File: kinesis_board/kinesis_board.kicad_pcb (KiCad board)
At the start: 0 parts

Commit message: finished drawing of the schematics -- needs to be checked before pcb drawing
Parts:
- added 16Mhz1: Crystal, Crystal:Crystal_SMD_HC49-SD_HandSoldering, F.Cu at (146.3, 96.3)
- added C1: 27p, Connector_JST:JST_PH_S7B-PH-K_1x07_P2.00mm_Horizontal, F.Cu at (138.6, 66.6)
- added C2: 27p, Capacitor_SMD:C_0805_2012Metric_Pad1.18x1.45mm_HandSolder, F.Cu at (160.7, 65.8)
- added C3: 100n, Capacitor_SMD:C_0805_2012Metric_Pad1.18x1.45mm_HandSolder, F.Cu at (160.7, 68.8)
- added C4: 4u7, Capacitor_SMD:C_0805_2012Metric_Pad1.18x1.45mm_HandSolder, F.Cu at (160.7, 71.8)
- added C5: 1u, Connector_JST:JST_PH_S7B-PH-K_1x07_P2.00mm_Horizontal, F.Cu at (138.6, 76.3)
- added FB1: FerriteBead, Inductor_SMD:L_0603_1608Metric_Pad1.05x0.95mm_HandSolder, F.Cu at (155.7, 89.4)
- added FB2: FerriteBead, Inductor_SMD:L_0603_1608Metric_Pad1.05x0.95mm_HandSolder, F.Cu at (155.7, 91.9)
- added J2: Conn_01x20, Connector_PinHeader_2.54mm:PinHeader_1x20_P2.54mm_Vertical_SMD_Pin1Left, F.Cu at (123.7, 90.7)
- added J3: Conn_01x20, Connector_PinHeader_2.54mm:PinHeader_1x20_P2.54mm_Vertical_SMD_Pin1Left, F.Cu at (131.6, 90.7)
- added J4: Conn_02x03_Odd_Even, Connector_IDC:IDC-Header_2x03_P2.54mm_Horizontal, F.Cu at (138.5, 105.6)
- added J5: Screw_Terminal_01x02, TerminalBlock_Phoenix:TerminalBlock_Phoenix_MPT-0,5-2-2.54_1x02_P2.54mm_Horizontal, F.Cu at (156.1, 80.2)
- added J6: Conn_01x07, Connector_JST:JST_PH_S7B-PH-K_1x07_P2.00mm_Horizontal, F.Cu at (138.6, 85.9)
- added R1: 68R, Resistor_SMD:R_0805_2012Metric_Pad1.20x1.40mm_HandSolder, F.Cu at (155.9, 65.7)
- added R2: 68R, Resistor_SMD:R_0805_2012Metric_Pad1.20x1.40mm_HandSolder, F.Cu at (155.9, 68.7)
- added R3: 1k5, Resistor_SMD:R_0805_2012Metric_Pad1.20x1.40mm_HandSolder, F.Cu at (155.9, 71.6)
- added R4: 4k7, Resistor_SMD:R_0805_2012Metric_Pad1.20x1.40mm_HandSolder, F.Cu at (155.9, 74.6)
- added TP1: TestPoint, TestPoint:TestPoint_Pad_2.0x2.0mm, F.Cu at (163.2, 78.1)
- added TP2: TestPoint, TestPoint:TestPoint_Pad_2.0x2.0mm, F.Cu at (163.2, 82.1)
- added U1: ATmega16-16A, Package_QFP:TQFP-44_10x10mm_P0.8mm, F.Cu at (160.0, 106.7)
- added U2: D1213A-04S, Package_TO_SOT_SMD:SOT-363_SC-70-6_Handsoldering, F.Cu at (156.5, 86.2)
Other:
- copper layers 0 -> 2

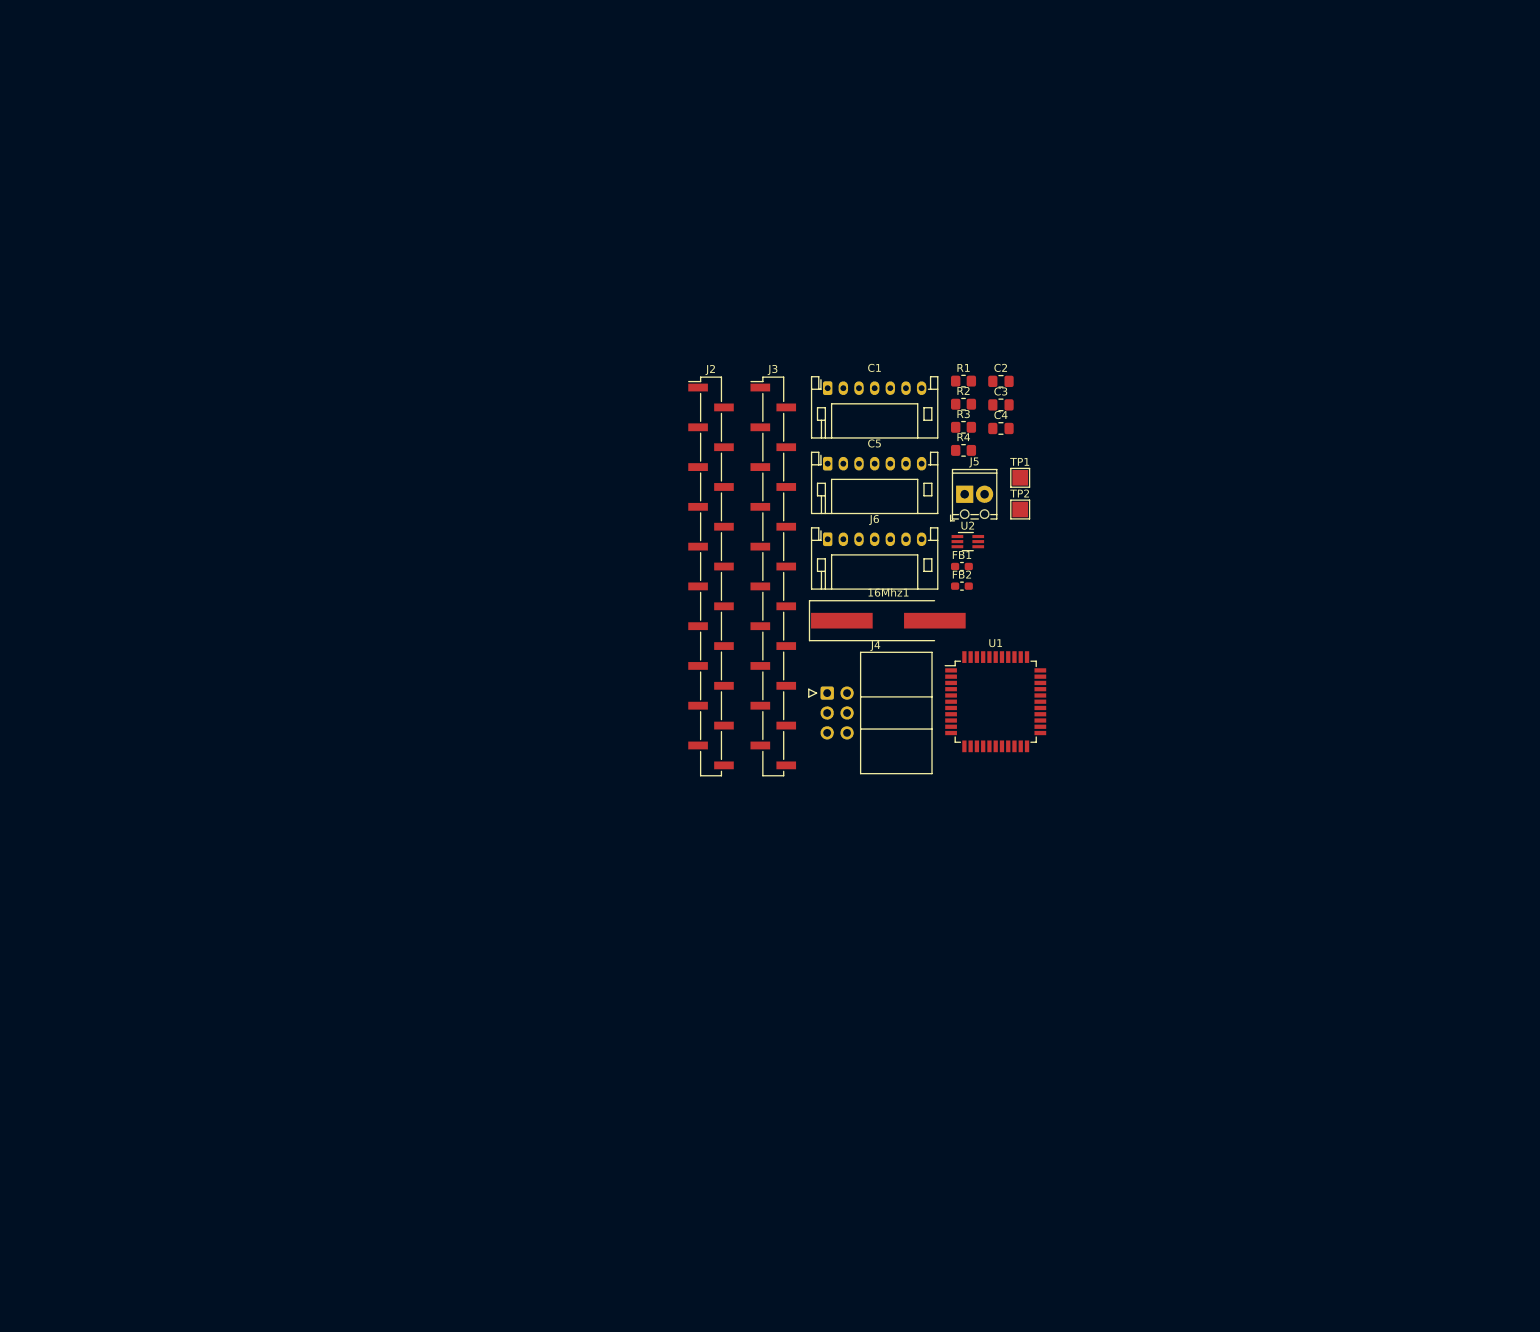
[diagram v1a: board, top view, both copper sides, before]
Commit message: first revision of board - routing needs to be optimized
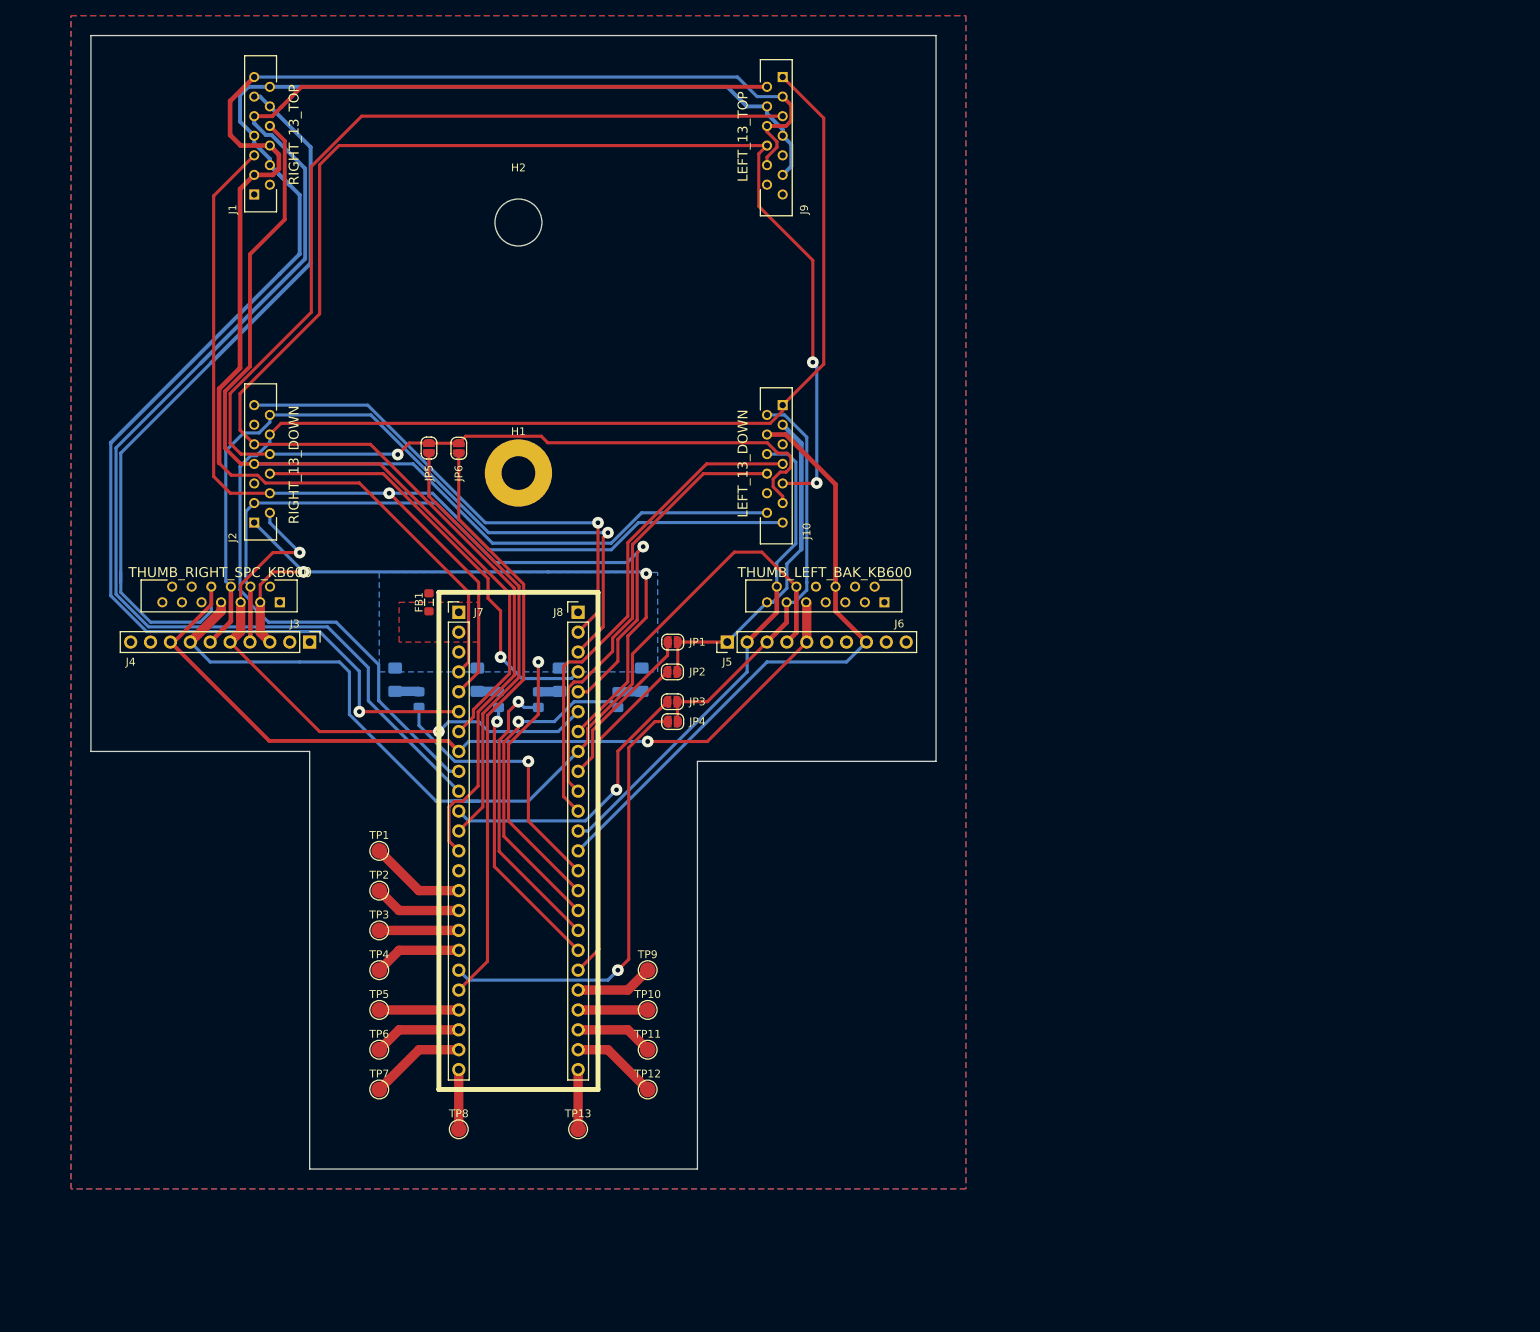
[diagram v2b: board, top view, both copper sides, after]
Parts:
- removed 16Mhz1: Crystal, Crystal:Crystal_SMD_HC49-SD_HandSoldering
- removed C1: 27p, Connector_JST:JST_PH_S7B-PH-K_1x07_P2.00mm_Horizontal
- removed C2: 27p, Capacitor_SMD:C_0805_2012Metric_Pad1.18x1.45mm_HandSolder
- removed C3: 100n, Capacitor_SMD:C_0805_2012Metric_Pad1.18x1.45mm_HandSolder
- removed C4: 4u7, Capacitor_SMD:C_0805_2012Metric_Pad1.18x1.45mm_HandSolder
- removed C5: 1u, Connector_JST:JST_PH_S7B-PH-K_1x07_P2.00mm_Horizontal
- removed FB2: FerriteBead, Inductor_SMD:L_0603_1608Metric_Pad1.05x0.95mm_HandSolder
- removed U1: ATmega16-16A, Package_QFP:TQFP-44_10x10mm_P0.8mm
- removed U2: D1213A-04S, Package_TO_SOT_SMD:SOT-363_SC-70-6_Handsoldering
- added H1: mounting pad, MountingHole:MountingHole_4.3mm_M4_Pad, F.Cu at (99.1, 77.5)
- added H2: mounting pad, MountingHole:MountingHole_6mm, F.Cu at (99.1, 45.5)
- added J1: RIGHT_13_TOP, dodo_conn:Molex-39-53-2135, F.Cu at (65.3, 41.9)
- added J10: LEFT_13_DOWN, dodo_conn:Molex-39-53-2135, F.Cu at (132.8, 68.8)
- added J7: LEFT_1x24, Connector_PinHeader_2.54mm:PinHeader_1x24_P2.54mm_Vertical, F.Cu at (91.4, 95.2)
- added J8: RIGHT_1x24, Connector_PinHeader_2.54mm:PinHeader_1x24_P2.54mm_Vertical, F.Cu at (106.7, 95.2)
- added J9: LEFT_13_TOP, dodo_conn:Molex-39-53-2135, F.Cu at (132.8, 26.9)
- added JP1: SolderJumper_2_Open, Jumper:SolderJumper-2_P1.3mm_Open_RoundedPad1.0x1.5mm, F.Cu at (118.8, 99.1)
- added JP2: SolderJumper_2_Open, Jumper:SolderJumper-2_P1.3mm_Open_RoundedPad1.0x1.5mm, F.Cu at (118.7, 102.9)
- added JP3: SolderJumper_2_Open, Jumper:SolderJumper-2_P1.3mm_Open_RoundedPad1.0x1.5mm, F.Cu at (118.7, 106.7)
- added JP4: SolderJumper_2_Open, Jumper:SolderJumper-2_P1.3mm_Open_RoundedPad1.0x1.5mm, F.Cu at (118.8, 109.2)
- added JP5: SolderJumper_2_Open, Jumper:SolderJumper-2_P1.3mm_Open_RoundedPad1.0x1.5mm, F.Cu at (87.6, 74.3)
- added JP6: SolderJumper_2_Open, Jumper:SolderJumper-2_P1.3mm_Open_RoundedPad1.0x1.5mm, F.Cu at (91.4, 74.3)
- added LED1: LEDSML1206, LED_SMD:LED_1206_3216Metric_Pad1.42x1.75mm_HandSolder, B.Cu at (114.8, 103.9)
- added LED2: LEDSML1206, LED_SMD:LED_1206_3216Metric_Pad1.42x1.75mm_HandSolder, B.Cu at (104.3, 103.9)
- added LED3: LEDSML1206, LED_SMD:LED_1206_3216Metric_Pad1.42x1.75mm_HandSolder, B.Cu at (93.8, 103.9)
- added LED4: LEDSML1206, LED_SMD:LED_1206_3216Metric_Pad1.42x1.75mm_HandSolder, B.Cu at (83.3, 103.9)
- added TP10: TX7, TestPoint:TestPoint_Pad_D2.0mm, F.Cu at (115.6, 146.1)
- added TP11: CRX3, TestPoint:TestPoint_Pad_D2.0mm, F.Cu at (115.6, 151.1)
- added TP12: CTX3, TestPoint:TestPoint_Pad_D2.0mm, F.Cu at (115.6, 156.2)
- added TP13: OUT1B, TestPoint:TestPoint_Pad_D2.0mm, F.Cu at (106.7, 161.3)
- added TP3: A15, TestPoint:TestPoint_Pad_D2.0mm, F.Cu at (81.3, 135.9)
- added TP4: A14, TestPoint:TestPoint_Pad_D2.0mm, F.Cu at (81.3, 141.0)
- added TP5: CS, TestPoint:TestPoint_Pad_D2.0mm, F.Cu at (81.3, 146.1)
- added TP6: TX8, TestPoint:TestPoint_Pad_D2.0mm, F.Cu at (81.3, 151.1)
- added TP7: RX8, TestPoint:TestPoint_Pad_D2.0mm, F.Cu at (81.3, 156.2)
- added TP8: MCLK2, TestPoint:TestPoint_Pad_D2.0mm, F.Cu at (91.4, 161.3)
- added TP9: RX7, TestPoint:TestPoint_Pad_D2.0mm, F.Cu at (115.6, 141.0)
- FB1: footprint Inductor_SMD:L_0603_1608Metric_Pad1.05x0.95mm_HandSolder -> Inductor_SMD:L_0805_2012Metric_Pad1.05x1.20mm_HandSolder
- J2: value Conn_01x20 -> RIGHT_13_DOWN; footprint Connector_PinHeader_2.54mm:PinHeader_1x20_P2.54mm_Vertical_SMD_Pin1Left -> dodo_conn:Molex-39-53-2135
- J3: value Conn_01x20 -> THUMB_RIGHT_SPC_KB600; footprint Connector_PinHeader_2.54mm:PinHeader_1x20_P2.54mm_Vertical_SMD_Pin1Left -> dodo_conn:Molex-39-53-2135
- J4: value Conn_02x03_Odd_Even -> THUMB_RIGHT_SPC; footprint Connector_IDC:IDC-Header_2x03_P2.54mm_Horizontal -> Connector_PinHeader_2.54mm:PinHeader_1x10_P2.54mm_Vertical
- J5: value Screw_Terminal_01x02 -> THUMB_LEFT_BAK; footprint TerminalBlock_Phoenix:TerminalBlock_Phoenix_MPT-0,5-2-2.54_1x02_P2.54mm_Horizontal -> Connector_PinHeader_2.54mm:PinHeader_1x10_P2.54mm_Vertical
- J6: value Conn_01x07 -> THUMB_LEFT_BAK_KB600; footprint Connector_JST:JST_PH_S7B-PH-K_1x07_P2.00mm_Horizontal -> dodo_conn:Molex-39-53-2135
- R1, R2: value 68R -> 10K; moved to B.Cu
- R3: value 1k5 -> 10K; moved to B.Cu
- R4: value 4k7 -> 10K; moved to B.Cu
- TP1: value TestPoint -> A17; footprint TestPoint:TestPoint_Pad_2.0x2.0mm -> TestPoint:TestPoint_Pad_D2.0mm
- TP2: value TestPoint -> A16; footprint TestPoint:TestPoint_Pad_2.0x2.0mm -> TestPoint:TestPoint_Pad_D2.0mm
- moved TP2 95.2 mm to (81.3, 130.8)
- moved TP1 94.7 mm to (81.3, 125.7)
- moved R4 76.5 mm to (86.4, 106.4), turned to 90 degrees
- moved R3 68.8 mm to (96.5, 106.4), turned to 90 degrees
- moved FB1 68.2 mm to (87.6, 94.0), turned to -90 degrees
- moved J4 66.4 mm to (72.4, 99.1), turned to -90 degrees
- moved R2 66.1 mm to (101.6, 106.4), turned to 90 degrees
- moved J3 63.1 mm to (68.6, 94.0), turned to 180 degrees
- moved R1 60.0 mm to (111.8, 106.4), turned to 90 degrees
- moved J2 58.8 mm to (65.3, 83.8), turned to 90 degrees
- moved J5 35.7 mm to (125.7, 99.1), turned to 90 degrees
- moved J6 10.8 mm to (145.8, 94.0), turned to 180 degrees
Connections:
- FB1 pad 1: +5V -> GND
- FB1 pad 2: Net-(J5-Pin_1) -> GNDA
- J2 pad 1: /NUM_LED -> /ROW_6
- J2 pad 10: unconnected-(J2-Pin_10) -> /COL_0
- J2 pad 12: unconnected-(J2-Pin_12) -> /ROW_9
- J2 pad 13: unconnected-(J2-Pin_13) -> /ROW_0
- J2 pad 2: /SCR_LED -> /ROW_8
- J2 pad 3: /KPD_LED -> /ROW_7
- J2 pad 4: /CAPS_LED -> /COL_4
- J2 pad 5: /KPD -> unconnected-(J2-Pin_5)
- J2 pad 6: /PGM -> /ROW_MIN
- J2 pad 7: /EEP_SCL -> /COL_3
- J2 pad 8: /EEP_SDA -> /COL_2
- J2 pad 9: GND -> /COL_1
- J3 pad 1: /MATRIX1 -> unconnected-(J3-Pin_1)
- J3 pad 12: /BUZZER -> unconnected-(J3-Pin_12)
- J3 pad 2: /MATRIX2 -> unconnected-(J3-Pin_2)
- J3 pad 3: /MATRIX3 -> /ROW_6
- J3 pad 4: /MATRIX4 -> /ROW_7
- J3 pad 5: /MATRIX5 -> /ROW_8
- J3 pad 6: /MATRIX6 -> /ROW_9
- J3 pad 7: /MATRIX7 -> /COL_6
- J3 pad 8: /MATRIX8 -> /COL_5
- J4 pad 1: /MISO -> unconnected-(J4-Pin_1)
- J4 pad 2: +5V -> unconnected-(J4-Pin_2)
- J4 pad 3: /SCK -> /ROW_6
- J4 pad 4: /MOSI -> /ROW_7
- J4 pad 5: /RST -> /ROW_8
- J4 pad 6: GND -> /ROW_9
- J5 pad 1: Net-(J5-Pin_1) -> /ROW_4
- J5 pad 2: GND -> /ROW_2
- J6 pad 1: /FS3 -> unconnected-(J6-Pin_1)
- J6 pad 2: Net-(J6-Pin_2) -> unconnected-(J6-Pin_2)
- J6 pad 3: /D+ -> unconnected-(J6-Pin_3)
- J6 pad 4: /D- -> unconnected-(J6-Pin_4)
- J6 pad 5: Net-(J5-Pin_1) -> unconnected-(J6-Pin_5)
- J6 pad 6: /FS1 -> /ROW_3
- J6 pad 7: /FS2 -> unconnected-(J6-Pin_7)
- R1 pad 1: /USB_D- -> /LED_KEYPAD
- R1 pad 2: /D- -> Net-(LED1-K)
- R2 pad 1: /D+ -> /LED_SCROLL_LOCK
- R2 pad 2: /USB_D+ -> Net-(LED2-K)
- R3 pad 1: +5V -> /LED_NUM_LOCK
- R3 pad 2: /D- -> Net-(LED3-K)
- R4 pad 1: +5V -> /LED_CAPS_LOCK
- R4 pad 2: /RST -> Net-(LED4-K)
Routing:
- net /COL_1: track 0.00 -> 228.8 mm, vias 0 -> 2
- net /ROW_F2: track 0.00 -> 213.6 mm, vias 0 -> 1
- net /COL_5: track 0.00 -> 202.4 mm, vias 0 -> 1
- net /ROW_ESC: track 0.00 -> 197.9 mm
- net /ROW_F1: track 0.00 -> 190.8 mm
- net /COL_2: track 0.00 -> 184.6 mm, vias 0 -> 1
- net /COL_3: track 0.00 -> 180.8 mm
- net /COL_0: track 0.00 -> 176.1 mm
- net /COL_4: track 0.00 -> 152.3 mm, vias 0 -> 1
- net /COL_6: track 0.00 -> 125.3 mm
- net /ROW_9: track 0.00 -> 100.1 mm, vias 0 -> 1
- net /ROW_7: track 0.00 -> 94.8 mm, vias 0 -> 1
- net /ROW_6: track 0.00 -> 90.6 mm, vias 0 -> 2
- net /ROW_3: track 0.00 -> 81.0 mm
- net /COL_2_JUMP1: track 0.00 -> 75.4 mm
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- added copper zone on B.Cu, net +3V3
- added copper zone on B.Cu, net GND
- added copper zone on F.Cu, net GND
- added copper zone on F.Cu, net GNDA
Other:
- board outline added: 108 x 144.8 mm

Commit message: adjusted placement of the pin headers and connectors - routing not finished
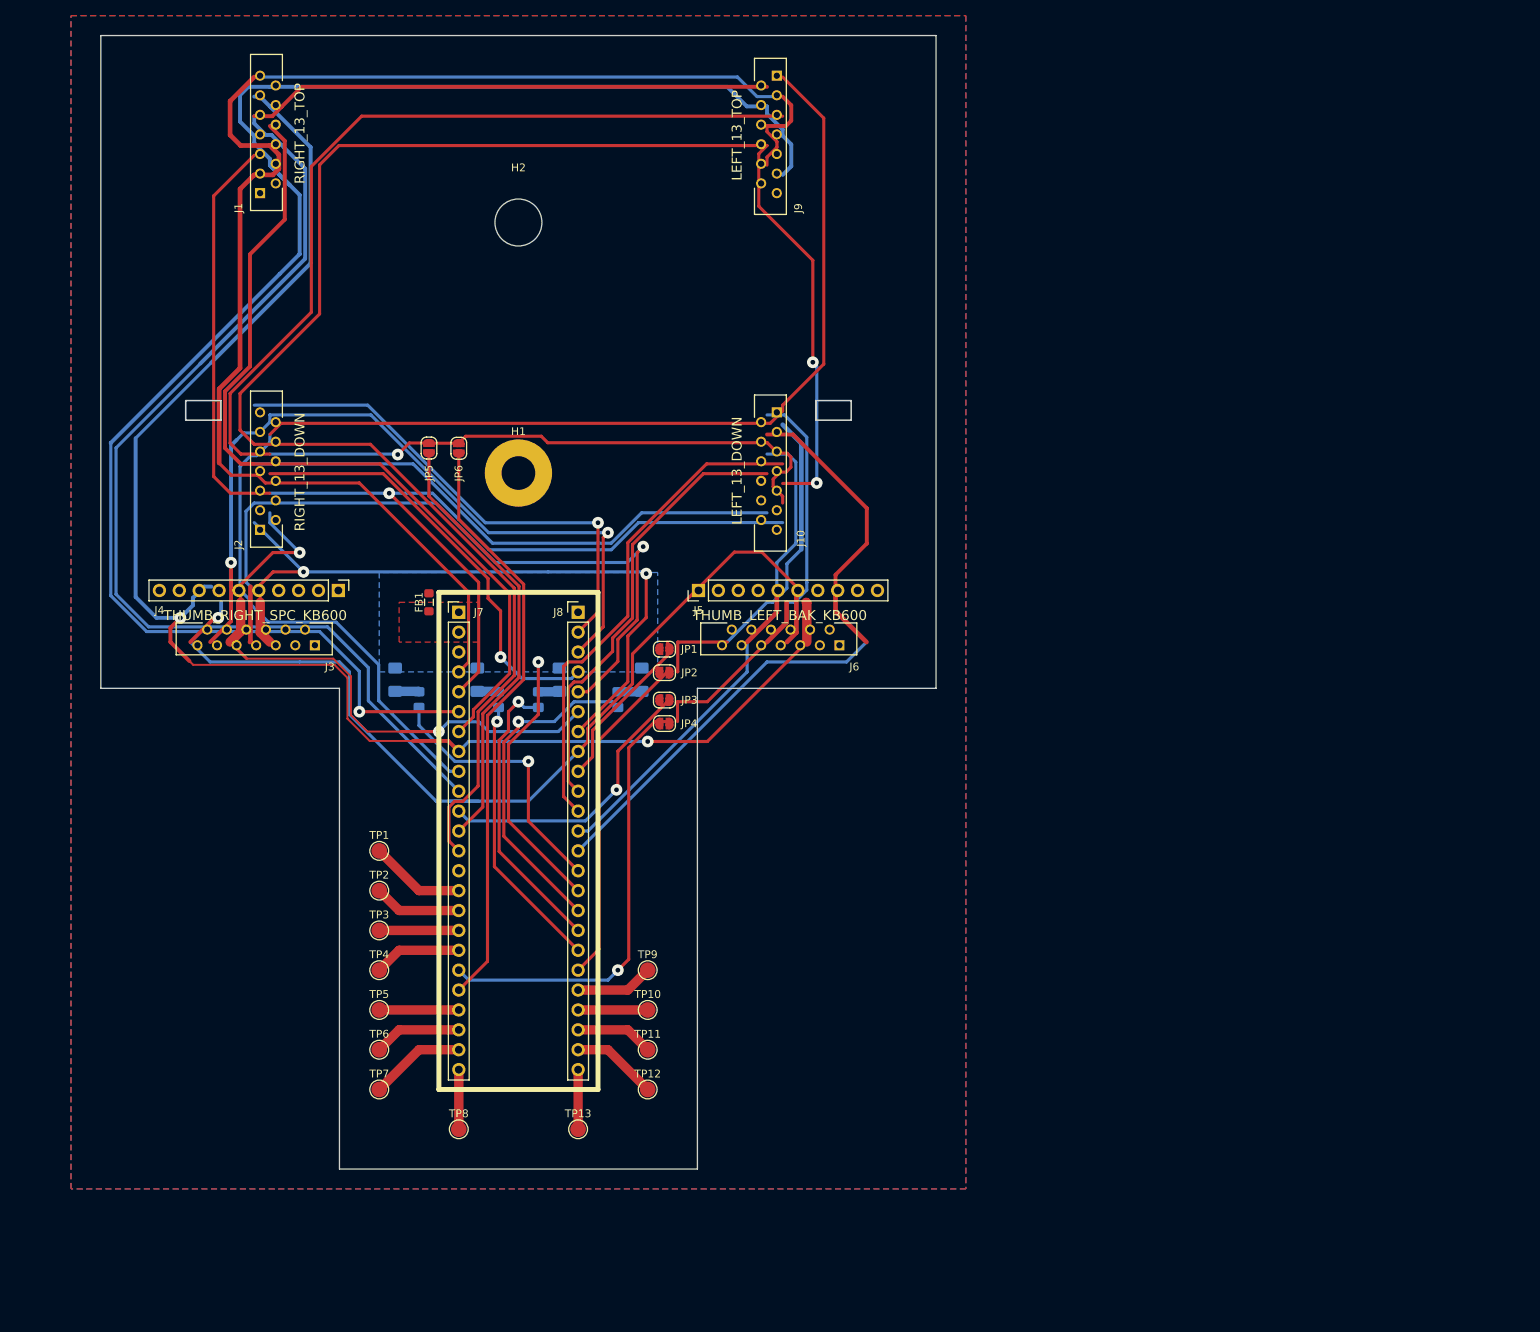
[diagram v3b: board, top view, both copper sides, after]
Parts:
- moved J6 7.95 mm to (140.1, 99.5)
- moved J4 7.54 mm to (76.1, 92.5)
- moved J5 7.54 mm to (122.1, 92.5)
- moved J3 7.09 mm to (73.1, 99.5)
- moved JP1 1.39 mm to (117.7, 100.0)
- moved J10 1.19 mm to (132.1, 69.7)
- moved J2 1.19 mm to (66.1, 84.7)
- moved JP4 1.08 mm to (117.7, 109.5)
- moved JP3 1.04 mm to (117.7, 106.5)
- moved JP2 1.02 mm to (117.7, 103.0)
- moved J1 0.77 mm to (66.1, 41.7)
- moved J9 0.77 mm to (132.1, 26.7)
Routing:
- net /ROW_2: track 63.5 -> 42.5 mm
- net /COL_5: track 202.4 -> 223.2 mm, vias 1 -> 2
- net /ROW_3: track 81.0 -> 68.9 mm
- net /ROW_5: track 52.2 -> 60.3 mm
- net /ROW_8: track 75.0 -> 78.0 mm
- net /ROW_9: track 100.1 -> 102.6 mm, vias 1 -> 2
- net /COL_6: track 125.3 -> 125.6 mm, vias 0 -> 1
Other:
- board size 108 x 144.8 mm -> 106.7 x 144.8 mm
